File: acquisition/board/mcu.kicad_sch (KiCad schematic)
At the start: 25 parts, among them J19 CONN_01X05, J20 CONN_01X06, Q1 SSM6N58NU, Q2 SSM6N58NU, U23 74AVCH1T45, U24 74AVCH1T45, U7 STM32L031-QFN32

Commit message: More power supply work, added PLL loop filter, soft start, began assigning footprints
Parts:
- C180: footprint (none) -> azonenberg_pcb:EIA_0603_CAP_NOSILK
- C181, C182, C183, C184, C185, C186, C187, C188: footprint (none) -> azonenberg_pcb:EIA_0402_CAP_NOSILK
- J19, TP8: footprint (none) -> azonenberg_pcb:CONN_HEADER_2.54MM_1x5
- J20: footprint (none) -> azonenberg_pcb:CONN_HEADER_2.54MM_1x6
- Q1, Q2: footprint (none) -> azonenberg_pcb:DFN_6_0.65MM_2x2MM_GDS
- R31, R32, R33: footprint (none) -> azonenberg_pcb:EIA_0402_RES_NOSILK
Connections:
- net PLL_SYNC: now also U7.14 (PB0); no longer U7.6 (PA0)
- new net VTEMP: U7.6 (PA0)
- no-connect marks 7 -> 6
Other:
- note added: "Vtemp is 150 mV @ 25C + 6.75 mV/C At 100C -> ~650 mV"
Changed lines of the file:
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@@
   (title_block
     (title "Digitizer board")
-    (date "2022-07-05")
+    (date "2022-07-08")
     (rev "0.1")
     (company "A. Zonenberg")
@@
   (no_connect (at 36.83 86.36))
   (no_connect (at 36.83 83.82))
-  (no_connect (at 36.83 81.28))
   (no_connect (at 36.83 111.76))
   (no_connect (at 88.9 142.24))
@@
     (effects (font (size 1.27 1.27)) (justify left bottom))
   )
+  (text "Vtemp is 150 mV @ 25C + 6.75 mV/C\nAt 100C -> ~650 mV"
+    (at 57.15 34.29 0)
+    (effects (font (size 1.27 1.27)) (justify left bottom))
+  )
   (label "MCU_SPI_SO" (at 88.9 83.82 180)
     (effects (font (size 1.27 1.27)) (justify right bottom))
@@
     (effects (font (size 1.27 1.27)) (justify right))
   )
-  (hierarchical_label "PLL_SYNC" (shape output) (at 36.83 31.75 180)
+  (hierarchical_label "PLL_SYNC" (shape output) (at 36.83 81.28 180)
     (effects (font (size 1.27 1.27)) (justify right))
   )
@@
   )
   (hierarchical_label "ADC2_PDWN" (shape output) (at 36.83 57.15 180)
+    (effects (font (size 1.27 1.27)) (justify right))
+  )
+  (hierarchical_label "VTEMP" (shape input) (at 36.83 31.75 180)
     (effects (font (size 1.27 1.27)) (justify right))
   )
@@
       (effects (font (size 1.27 1.27)) (justify left))
     )
-    (property "Footprint" "" (id 2) (at 54.3052 177.8 0)
+    (property "Footprint" "azonenberg_pcb:EIA_0402_CAP_NOSILK" (id 2) (at 54.3052 177.8 0)
       (effects (font (size 1.27 1.27)) hide)
     )
@@
       (effects (font (size 1.27 1.27)) (justify left))
     )
-    (property "Footprint" "" (id 2) (at 46.6852 163.83 0)
+    (property "Footprint" "azonenberg_pcb:EIA_0402_CAP_NOSILK" (id 2) (at 46.6852 163.83 0)
       (effects (font (size 1.27 1.27)) hide)
     )
@@
     (property "Reference" "R31" (id 0) (at 33.02 144.78 90))
     (property "Value" "0" (id 1) (at 33.02 142.24 90))
-    (property "Footprint" "" (id 2) (at 33.02 144.018 90)
+    (property "Footprint" "azonenberg_pcb:EIA_0402_RES_NOSILK" (id 2) (at 33.02 144.018 90)
       (effects (font (size 1.27 1.27)) hide)
     )
@@
       (effects (font (size 1.27 1.27)) (justify left))
     )
-    (property "Footprint" "" (id 2) (at 26.3652 177.8 0)
+    (property "Footprint" "azonenberg_pcb:EIA_0603_CAP_NOSILK" (id 2) (at 26.3652 177.8 0)
       (effects (font (size 1.27 1.27)) hide)
     )
@@
       (effects (font (size 1.27 1.27)) (justify left))
     )
-    (property "Footprint" "" (id 2) (at 148.2852 180.34 0)
+    (property "Footprint" "azonenberg_pcb:EIA_0402_CAP_NOSILK" (id 2) (at 148.2852 180.34 0)
       (effects (font (size 1.27 1.27)) hide)
     )
@@
       (effects (font (size 1.27 1.27)) (justify left))
     )
-    (property "Footprint" "" (id 2) (at 40.3352 177.8 0)
+    (property "Footprint" "azonenberg_pcb:EIA_0402_CAP_NOSILK" (id 2) (at 40.3352 177.8 0)
       (effects (font (size 1.27 1.27)) hide)
     )
@@
       (effects (font (size 1.27 1.27)) (justify left))
     )
-    (property "Footprint" "" (id 2) (at 163.5252 167.64 0)
+    (property "Footprint" "azonenberg_pcb:EIA_0402_CAP_NOSILK" (id 2) (at 163.5252 167.64 0)
       (effects (font (size 1.27 1.27)) hide)
     )
@@
       (effects (font (size 1.27 1.27)) (justify left))
     )
-    (property "Footprint" "" (id 2) (at 92.202 162.56 90)
+    (property "Footprint" "azonenberg_pcb:EIA_0402_RES_NOSILK" (id 2) (at 92.202 162.56 90)
       (effects (font (size 1.27 1.27)) hide)
     )
@@
       (effects (font (size 1.524 1.524)) (justify left))
     )
-    (property "Footprint" "" (id 2) (at 140.97 50.8 0)
-      (effects (font (size 1.524 1.524)))
+    (property "Footprint" "azonenberg_pcb:DFN_6_0.65MM_2x2MM_GDS" (id 2) (at 140.97 50.8 0)
+      (effects (font (size 1.524 1.524)) hide)
     )
     (property "Datasheet" "transistors/mos/*.*" (id 3) (at 144.2466 54.6538 0)
@@
       (effects (font (size 1.27 1.27)) (justify left))
     )
-    (property "Footprint" "" (id 2) (at 68.2752 177.8 0)
+    (property "Footprint" "azonenberg_pcb:EIA_0402_CAP_NOSILK" (id 2) (at 68.2752 177.8 0)
       (effects (font (size 1.27 1.27)) hide)
     )
@@
       (effects (font (size 1.27 1.27)) (justify left))
     )
-    (property "Footprint" "" (id 2) (at 93.98 83.82 0)
+    (property "Footprint" "azonenberg_pcb:CONN_HEADER_2.54MM_1x5" (id 2) (at 93.98 83.82 0)
       (effects (font (size 1.27 1.27)) hide)
     )
@@
       (effects (font (size 1.524 1.524)) (justify left))
     )
-    (property "Footprint" "" (id 2) (at 111.76 50.8 0)
-      (effects (font (size 1.524 1.524)))
+    (property "Footprint" "azonenberg_pcb:DFN_6_0.65MM_2x2MM_GDS" (id 2) (at 111.76 50.8 0)
+      (effects (font (size 1.524 1.524)) hide)
     )
     (property "Datasheet" "transistors/mos/*.*" (id 3) (at 115.0366 54.6538 0)
@@
       (effects (font (size 1.524 1.524)) (justify left))
     )
-    (property "Footprint" "" (id 2) (at 199.39 50.8 0)
-      (effects (font (size 1.524 1.524)))
+    (property "Footprint" "azonenberg_pcb:DFN_6_0.65MM_2x2MM_GDS" (id 2) (at 199.39 50.8 0)
+      (effects (font (size 1.524 1.524)) hide)
     )
     (property "Datasheet" "transistors/mos/*.*" (id 3) (at 202.6666 54.6538 0)
@@
       (effects (font (size 1.27 1.27)) (justify left))
     )
-    (property "Footprint" "" (id 2) (at 93.98 135.89 0)
+    (property "Footprint" "azonenberg_pcb:CONN_HEADER_2.54MM_1x6" (id 2) (at 93.98 135.89 0)
       (effects (font (size 1.27 1.27)) hide)
     )
@@
       (effects (font (size 1.27 1.27)) (justify left))
     )
-    (property "Footprint" "" (id 2) (at 148.2852 167.64 0)
+    (property "Footprint" "azonenberg_pcb:EIA_0402_CAP_NOSILK" (id 2) (at 148.2852 167.64 0)
       (effects (font (size 1.27 1.27)) hide)
     )
@@
       (effects (font (size 1.27 1.27)) (justify left))
     )
-    (property "Footprint" "" (id 2) (at 35.052 160.02 90)
+    (property "Footprint" "azonenberg_pcb:EIA_0402_RES_NOSILK" (id 2) (at 35.052 160.02 90)
       (effects (font (size 1.27 1.27)) hide)
     )
@@
       (effects (font (size 1.27 1.27)) (justify left))
     )
-    (property "Footprint" "" (id 2) (at 93.98 106.68 0)
+    (property "Footprint" "azonenberg_pcb:CONN_HEADER_2.54MM_1x5" (id 2) (at 93.98 106.68 0)
       (effects (font (size 1.27 1.27)) hide)
     )
@@
       (effects (font (size 1.524 1.524)) (justify left))
     )
-    (property "Footprint" "" (id 2) (at 170.18 50.8 0)
-      (effects (font (size 1.524 1.524)))
+    (property "Footprint" "azonenberg_pcb:DFN_6_0.65MM_2x2MM_GDS" (id 2) (at 170.18 50.8 0)
+      (effects (font (size 1.524 1.524)) hide)
     )
     (property "Datasheet" "transistors/mos/*.*" (id 3) (at 173.4566 54.6538 0)
@@
       (effects (font (size 1.27 1.27)) (justify left))
     )
-    (property "Footprint" "" (id 2) (at 163.5252 180.34 0)
-      (effects (font (size 1.27 1.27)) hide)
-    )
+    (property "Footprint" "azonenberg_pcb:EIA_0402_CAP_NOSILK" (id 2) (at 163.5252 180.34 0)
+      (effects (font (size 1.27 1.27)) hide)
+    )

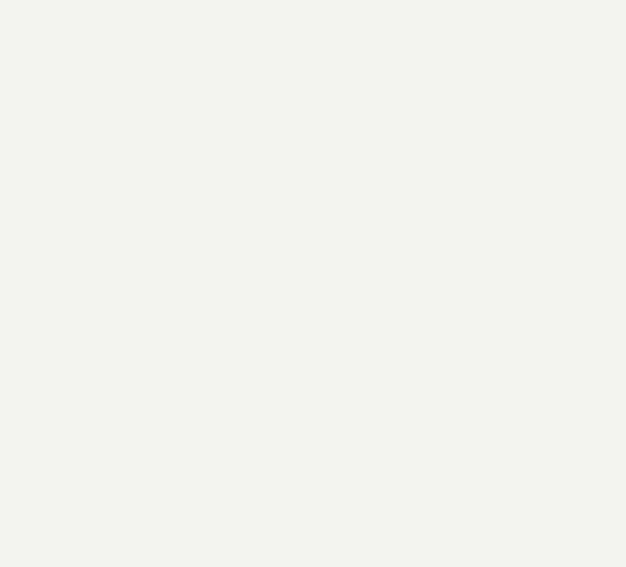
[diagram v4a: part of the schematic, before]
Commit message: Completed schematic after design review, ready for layout
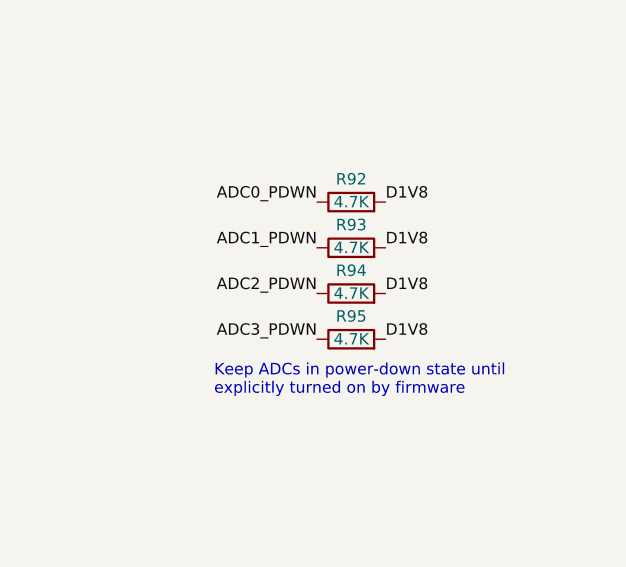
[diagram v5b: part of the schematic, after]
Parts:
- added R92, R93, R94, R95: 4.7K, symbol device:R
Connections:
- net ADC0_PDWN: now also R92.1
- net ADC1_PDWN: now also R93.1
- net ADC2_PDWN: now also R94.1
- net ADC3_PDWN: now also R95.1
- net D1V8: now also R92.2, R93.2, R94.2, R95.2
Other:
- note added: "Keep ADCs in power-down state until explicitly turned on by firmware"
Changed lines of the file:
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@@
   (title_block
     (title "Digitizer board")
-    (date "2022-07-08")
+    (date "2022-07-17")
     (rev "0.1")
     (company "A. Zonenberg")
@@
     (stroke (width 0) (type default) (color 0 0 0 0))
   )
+  (text "Keep ADCs in power-down state until\nexplicitly turned on by firmware"
+    (at 208.28 156.21 0)
+    (effects (font (size 1.27 1.27)) (justify left bottom))
+  )
   (text "SWD programming/debug header\nfor use with ST-Link v2\n1.8V logic levels"
     (at 92.71 119.38 0)
@@
     (effects (font (size 1.27 1.27)) (justify right bottom))
   )
+  (label "D1V8" (at 227.33 139.7 0)
+    (effects (font (size 1.27 1.27)) (justify left bottom))
+  )
+  (label "ADC1_PDWN" (at 219.71 139.7 180)
+    (effects (font (size 1.27 1.27)) (justify right bottom))
+  )
+  (label "D1V8" (at 227.33 134.62 0)
+    (effects (font (size 1.27 1.27)) (justify left bottom))
+  )
   (label "D1V8" (at 142.24 147.32 180)
     (effects (font (size 1.27 1.27)) (justify right bottom))
@@
     (effects (font (size 1.27 1.27)) (justify right bottom))
   )
+  (label "ADC3_PDWN" (at 219.71 149.86 180)
+    (effects (font (size 1.27 1.27)) (justify right bottom))
+  )
   (label "SWD_SWCLK" (at 88.9 106.68 180)
     (effects (font (size 1.27 1.27)) (justify right bottom))
@@
     (effects (font (size 1.27 1.27)) (justify right bottom))
   )
+  (label "ADC0_PDWN" (at 219.71 134.62 180)
+    (effects (font (size 1.27 1.27)) (justify right bottom))
+  )
   (label "GND" (at 168.91 133.35 0)
     (effects (font (size 1.27 1.27)) (justify left bottom))
@@
     (effects (font (size 1.27 1.27)) (justify right bottom))
   )
+  (label "D1V8" (at 227.33 149.86 0)
+    (effects (font (size 1.27 1.27)) (justify left bottom))
+  )
+  (label "ADC2_PDWN" (at 219.71 144.78 180)
+    (effects (font (size 1.27 1.27)) (justify right bottom))
+  )
   (label "UART_TX_3V3" (at 168.91 154.94 0)
     (effects (font (size 1.27 1.27)) (justify left bottom))
@@
   (label "GND" (at 114.3 59.69 180)
     (effects (font (size 1.27 1.27)) (justify right bottom))
+  )
+  (label "D1V8" (at 227.33 144.78 0)
+    (effects (font (size 1.27 1.27)) (justify left bottom))
   )
   (hierarchical_label "FPGA_DONE" (shape input) (at 36.83 91.44 180)
@@
     (pin "5")
     (pin "6")
+  )
+  (symbol (lib_id "device:R") (at 223.52 149.86 90) (unit 1)
+    (in_bom yes) (on_board yes)
+    (property "Reference" "R95" (id 0) (at 223.52 147.32 90))
+    (property "Value" "4.7K" (id 1) (at 223.52 149.86 90))
+    (property "Footprint" "" (id 2) (at 223.52 151.638 90)
+      (effects (font (size 1.27 1.27)) hide)
+    )
+    (property "Datasheet" "" (id 3) (at 223.52 149.86 0)
+      (effects (font (size 1.27 1.27)) hide)
+    )
+    (pin "1")
+    (pin "2")
   )
   (symbol (lib_id "st-azonenberg:STM32L031-QFN32") (at 40.64 115.57 0) (unit 3)
@@
     )
     (property "Datasheet" "" (id 3) (at 147.32 176.53 0)
+      (effects (font (size 1.27 1.27)) hide)
+    )
+    (pin "1")
+    (pin "2")
+  )
+  (symbol (lib_id "device:R") (at 223.52 144.78 90) (unit 1)
+    (in_bom yes) (on_board yes)
+    (property "Reference" "R94" (id 0) (at 223.52 142.24 90))
+    (property "Value" "4.7K" (id 1) (at 223.52 144.78 90))
+    (property "Footprint" "" (id 2) (at 223.52 146.558 90)
+      (effects (font (size 1.27 1.27)) hide)
+    )
+    (property "Datasheet" "" (id 3) (at 223.52 144.78 0)
       (effects (font (size 1.27 1.27)) hide)
     )
@@
     (pin "S2")
   )
+  (symbol (lib_id "device:R") (at 223.52 139.7 90) (unit 1)
+    (in_bom yes) (on_board yes)
+    (property "Reference" "R93" (id 0) (at 223.52 137.16 90))
+    (property "Value" "4.7K" (id 1) (at 223.52 139.7 90))
+    (property "Footprint" "" (id 2) (at 223.52 141.478 90)
+      (effects (font (size 1.27 1.27)) hide)
+    )
+    (property "Datasheet" "" (id 3) (at 223.52 139.7 0)
+      (effects (font (size 1.27 1.27)) hide)
+    )
+    (pin "1")
+    (pin "2")
+  )
   (symbol (lib_id "conn:CONN_01X06") (at 93.98 135.89 0) (unit 1)
     (in_bom yes) (on_board yes) (fields_autoplaced)
@@
       (effects (font (size 1.27 1.27)) hide)
     )
+    (pin "1")
+    (pin "2")
+  )
+  (symbol (lib_id "device:R") (at 223.52 134.62 90) (unit 1)
+    (in_bom yes) (on_board yes)
+    (property "Reference" "R92" (id 0) (at 223.52 132.08 90))
+    (property "Value" "4.7K" (id 1) (at 223.52 134.62 90))
+    (property "Footprint" "" (id 2) (at 223.52 136.398 90)
+      (effects (font (size 1.27 1.27)) hide)
+    )
+    (property "Datasheet" "" (id 3) (at 223.52 134.62 0)
+      (effects (font (size 1.27 1.27)) hide)
+    )

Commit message: Finished footprint assignment
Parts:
- D20, D21, D22, D23, D24: footprint (none) -> azonenberg_pcb:EIA_0603_LED
- R92, R93, R94, R95: footprint (none) -> azonenberg_pcb:EIA_0402_RES_NOSILK
- U23, U24: footprint (none) -> azonenberg_pcb:DFN_6_0.5MM_1.45x1.00MM
- U7: footprint (none) -> azonenberg_pcb:QFN_32_0.5MM_5x5MM
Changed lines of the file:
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@@
   (title_block
     (title "Digitizer board")
-    (date "2022-07-17")
+    (date "2023-01-29")
     (rev "0.1")
     (company "A. Zonenberg")
@@
       (effects (font (size 1.524 1.524)))
     )
-    (property "Footprint" "" (id 2) (at 147.32 139.7 0)
+    (property "Footprint" "azonenberg_pcb:DFN_6_0.5MM_1.45x1.00MM" (id 2) (at 147.32 139.7 0)
       (effects (font (size 1.524 1.524)) hide)
     )
@@
     (property "Reference" "R95" (id 0) (at 223.52 147.32 90))
     (property "Value" "4.7K" (id 1) (at 223.52 149.86 90))
-    (property "Footprint" "" (id 2) (at 223.52 151.638 90)
+    (property "Footprint" "azonenberg_pcb:EIA_0402_RES_NOSILK" (id 2) (at 223.52 151.638 90)
       (effects (font (size 1.27 1.27)) hide)
     )
@@
       (effects (font (size 1.27 1.27)) (justify left))
     )
-    (property "Footprint" "" (id 2) (at 40.64 115.57 0)
+    (property "Footprint" "azonenberg_pcb:QFN_32_0.5MM_5x5MM" (id 2) (at 40.64 115.57 0)
       (effects (font (size 1.27 1.27)) hide)
     )
@@
       (effects (font (size 1.27 1.27)) (justify left))
     )
-    (property "Footprint" "" (id 2) (at 40.64 143.51 0)
+    (property "Footprint" "azonenberg_pcb:QFN_32_0.5MM_5x5MM" (id 2) (at 40.64 143.51 0)
       (effects (font (size 1.27 1.27)) hide)
     )
@@
       (effects (font (size 1.27 1.27)) (justify right))
     )
-    (property "Footprint" "" (id 2) (at 93.98 170.18 0)
+    (property "Footprint" "azonenberg_pcb:EIA_0603_LED" (id 2) (at 93.98 170.18 0)
       (effects (font (size 1.27 1.27)) hide)
     )
@@
     (property "Reference" "R94" (id 0) (at 223.52 142.24 90))
     (property "Value" "4.7K" (id 1) (at 223.52 144.78 90))
-    (property "Footprint" "" (id 2) (at 223.52 146.558 90)
+    (property "Footprint" "azonenberg_pcb:EIA_0402_RES_NOSILK" (id 2) (at 223.52 146.558 90)
       (effects (font (size 1.27 1.27)) hide)
     )
@@
       (effects (font (size 1.27 1.27)) (justify left))
     )
-    (property "Footprint" "" (id 2) (at 40.64 71.12 0)
+    (property "Footprint" "azonenberg_pcb:QFN_32_0.5MM_5x5MM" (id 2) (at 40.64 71.12 0)
       (effects (font (size 1.27 1.27)) hide)
     )
@@
     (property "Reference" "R93" (id 0) (at 223.52 137.16 90))
     (property "Value" "4.7K" (id 1) (at 223.52 139.7 90))
-    (property "Footprint" "" (id 2) (at 223.52 141.478 90)
+    (property "Footprint" "azonenberg_pcb:EIA_0402_RES_NOSILK" (id 2) (at 223.52 141.478 90)
       (effects (font (size 1.27 1.27)) hide)
     )
@@
       (effects (font (size 1.27 1.27)) (justify left))
     )
-    (property "Footprint" "" (id 2) (at 40.64 102.87 0)
+    (property "Footprint" "azonenberg_pcb:QFN_32_0.5MM_5x5MM" (id 2) (at 40.64 102.87 0)
       (effects (font (size 1.27 1.27)) hide)
     )
@@
       (effects (font (size 1.524 1.524)))
     )
-    (property "Footprint" "" (id 2) (at 147.32 156.21 0)
+    (property "Footprint" "azonenberg_pcb:DFN_6_0.5MM_1.45x1.00MM" (id 2) (at 147.32 156.21 0)
       (effects (font (size 1.524 1.524)) hide)
     )
@@
       (effects (font (size 1.27 1.27)) (justify right))
     )
-    (property "Footprint" "" (id 2) (at 172.72 41.91 0)
+    (property "Footprint" "azonenberg_pcb:EIA_0603_LED" (id 2) (at 172.72 41.91 0)
       (effects (font (size 1.27 1.27)) hide)
     )
@@
       (effects (font (size 1.27 1.27)) (justify right))
     )
-    (property "Footprint" "" (id 2) (at 201.93 41.91 0)
+    (property "Footprint" "azonenberg_pcb:EIA_0603_LED" (id 2) (at 201.93 41.91 0)
       (effects (font (size 1.27 1.27)) hide)
     )
@@
       (effects (font (size 1.27 1.27)) (justify right))
     )
-    (property "Footprint" "" (id 2) (at 143.51 41.91 0)
+    (property "Footprint" "azonenberg_pcb:EIA_0603_LED" (id 2) (at 143.51 41.91 0)
       (effects (font (size 1.27 1.27)) hide)
     )
@@
     (property "Reference" "R92" (id 0) (at 223.52 132.08 90))
     (property "Value" "4.7K" (id 1) (at 223.52 134.62 90))
-    (property "Footprint" "" (id 2) (at 223.52 136.398 90)
+    (property "Footprint" "azonenberg_pcb:EIA_0402_RES_NOSILK" (id 2) (at 223.52 136.398 90)
       (effects (font (size 1.27 1.27)) hide)
     )
@@
       (effects (font (size 1.27 1.27)) (justify right))
     )
-    (property "Footprint" "" (id 2) (at 114.3 41.91 0)
-      (effects (font (size 1.27 1.27)) hide)
-    )
+    (property "Footprint" "azonenberg_pcb:EIA_0603_LED" (id 2) (at 114.3 41.91 0)
+      (effects (font (size 1.27 1.27)) hide)
+    )
